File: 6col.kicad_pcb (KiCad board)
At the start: 2 copper layers, 135.3 x 94.8 mm, 48 parts, among them K1 KEYSW, K10 KEYSW, K11 KEYSW, K12 KEYSW, K13 KEYSW, K14 KEYSW, K15 KEYSW, K16 KEYSW, K17 KEYSW, K18 KEYSW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

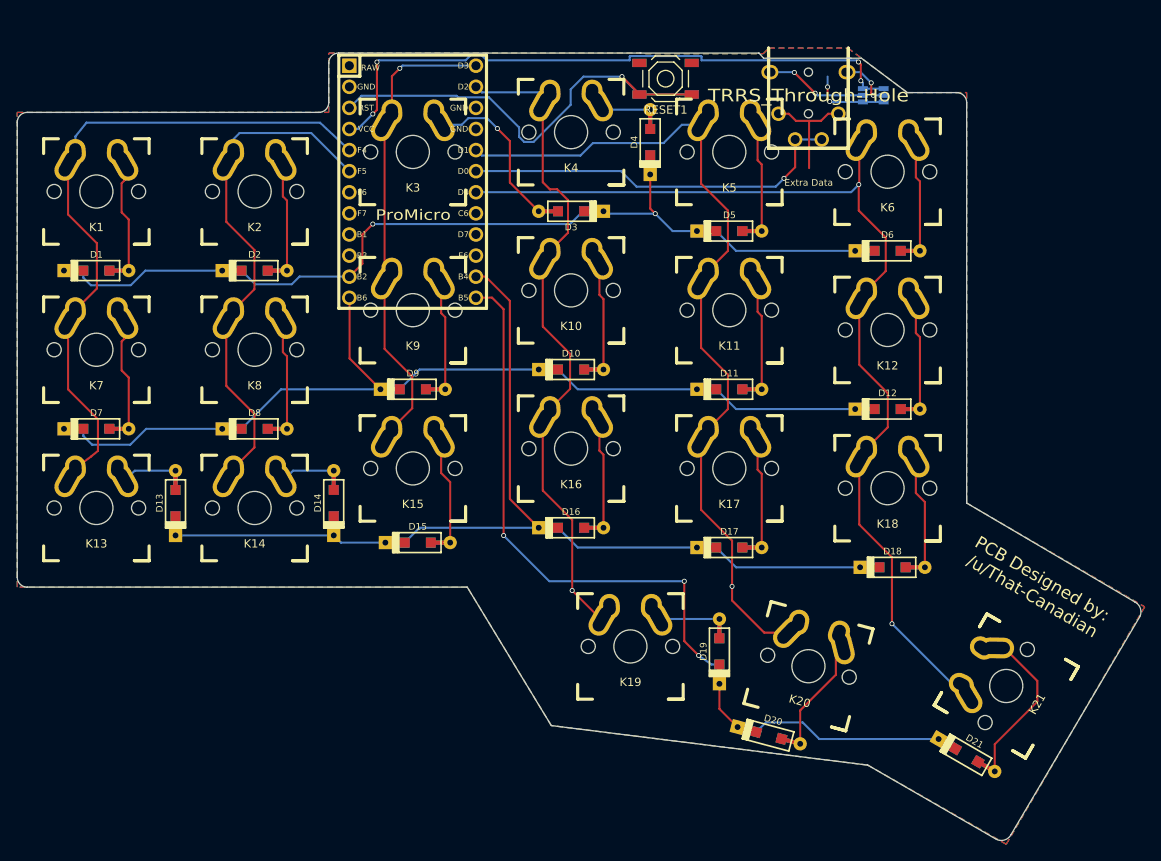
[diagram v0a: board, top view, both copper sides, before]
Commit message: WIP on Kailh sockets support
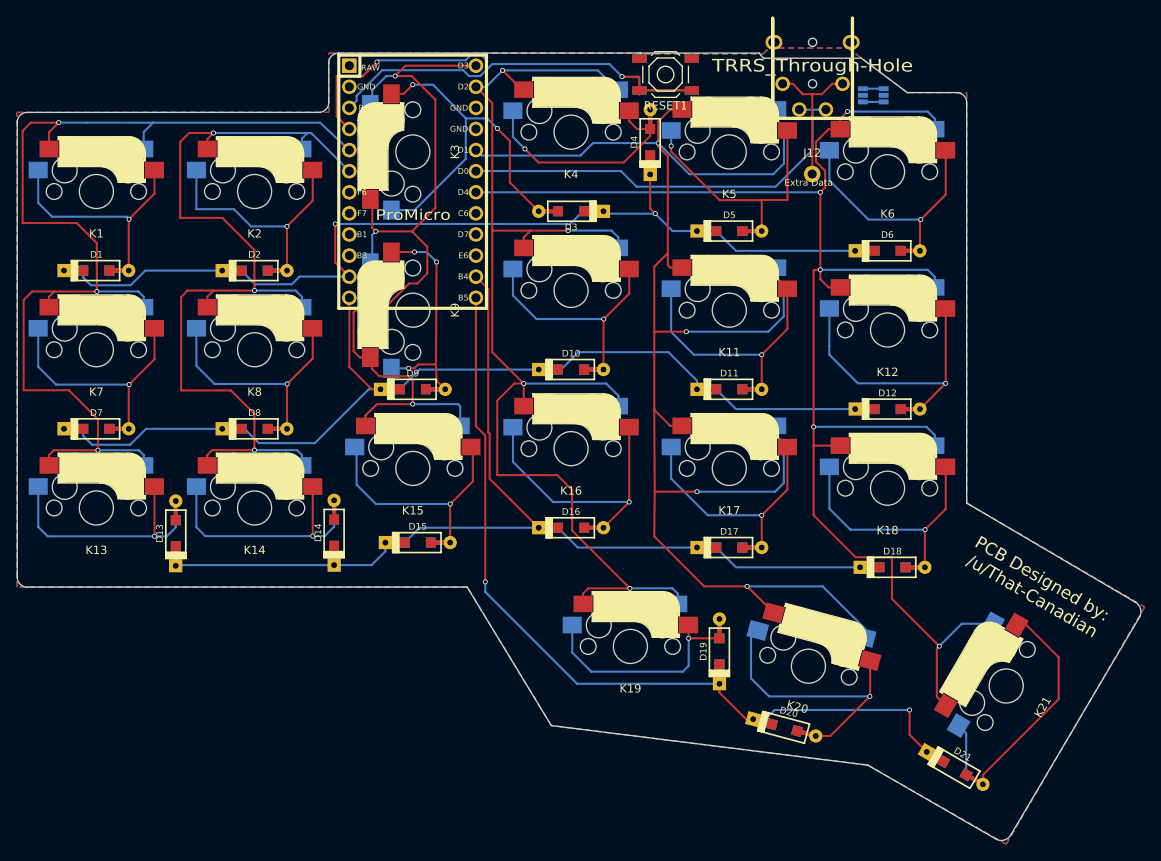
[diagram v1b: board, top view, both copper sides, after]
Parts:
- added J12: CONN_01X01_FEMALE, canadian_footprints:SolderWirePad_single_0-8mmDrill, F.Cu at (154.2, 68.9)
- K1, K10, K11, K12, K13, K14, K15, K16, K17, K18, K19, K2, K20, K3, K4, K5, K6, K7, K8, K9: value KEYSW -> KAILH_SK; footprint canadian_footprints:Mx_Alps_100-dualside -> kbd:CherryMX_Hotswap_lrn
- K21: value KEYSW -> KAILH_SK; footprint canadian_footprints:Mx_Alps_175-dualside -> kbd:CherryMX_Hotswap_lrn
- moved D13 3.65 mm to (77.5, 112.1)
- moved K22 3.63 mm to (154.2, 50.1)
- moved D14 3.57 mm to (96.6, 112.0)
- moved D21 2.11 mm to (171.3, 140.4)
- moved D20 2.10 mm to (150.8, 135.5)
- moved RESET1 0.50 mm to (136.5, 56.9) (x2)
- turned K3 to 90 degrees
- turned K9 to 90 degrees
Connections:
- K1 pad 1: /col1 -> Net-(D1-Pad2)
- K1 pad 2: Net-(D1-Pad2) -> /col1
- K10 pad 1: /col4 -> Net-(D10-Pad2)
- K10 pad 2: Net-(D10-Pad2) -> /col4
- K11 pad 1: /col5 -> Net-(D11-Pad2)
- K11 pad 2: Net-(D11-Pad2) -> /col5
- K12 pad 1: /col6 -> Net-(D12-Pad2)
- K12 pad 2: Net-(D12-Pad2) -> /col6
- K13 pad 1: /col1 -> Net-(D13-Pad2)
- K13 pad 2: Net-(D13-Pad2) -> /col1
- K14 pad 1: /col2 -> Net-(D14-Pad2)
- K14 pad 2: Net-(D14-Pad2) -> /col2
- K15 pad 1: /col3 -> Net-(D15-Pad2)
- K15 pad 2: Net-(D15-Pad2) -> /col3
- K16 pad 1: /col4 -> Net-(D16-Pad2)
- K16 pad 2: Net-(D16-Pad2) -> /col4
- K17 pad 1: /col5 -> Net-(D17-Pad2)
- K17 pad 2: Net-(D17-Pad2) -> /col5
- K18 pad 1: /col6 -> Net-(D18-Pad2)
- K18 pad 2: Net-(D18-Pad2) -> /col6
- K19 pad 1: /col4 -> Net-(D19-Pad2)
- K19 pad 2: Net-(D19-Pad2) -> /col4
- K2 pad 1: /col2 -> Net-(D2-Pad2)
- K2 pad 2: Net-(D2-Pad2) -> /col2
- K20 pad 1: /col5 -> Net-(D20-Pad2)
- K20 pad 2: Net-(D20-Pad2) -> /col5
- K21 pad 1: /col6 -> Net-(D21-Pad2)
- K21 pad 2: Net-(D21-Pad2) -> /col6
- K3 pad 1: /col3 -> Net-(D3-Pad2)
- K3 pad 2: Net-(D3-Pad2) -> /col3
- K4 pad 1: /col4 -> Net-(D4-Pad2)
- K4 pad 2: Net-(D4-Pad2) -> /col4
- K5 pad 1: /col5 -> Net-(D5-Pad2)
- K5 pad 2: Net-(D5-Pad2) -> /col5
- K6 pad 1: /col6 -> Net-(D6-Pad2)
- K6 pad 2: Net-(D6-Pad2) -> /col6
- K7 pad 1: /col1 -> Net-(D7-Pad2)
- K7 pad 2: Net-(D7-Pad2) -> /col1
- K8 pad 1: /col2 -> Net-(D8-Pad2)
- K8 pad 2: Net-(D8-Pad2) -> /col2
- K9 pad 1: /col3 -> Net-(D9-Pad2)
- K9 pad 2: Net-(D9-Pad2) -> /col3
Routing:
- net /col5: track 97.6 -> 190.5 mm, vias 1 -> 4
- net /col4: track 76.2 -> 147.8 mm, vias 1 -> 4
- net /col6: track 119.9 -> 184.8 mm, vias 2 -> 5
- net /col1: track 77.3 -> 133.1 mm, vias 0 -> 3
- net /col2: track 57.6 -> 110.9 mm, vias 0 -> 3
- net VCC: track 75.6 -> 28.9 mm, vias 4 -> 1
- net /col3: track 54.0 -> 100.1 mm, vias 1 -> 3
- net Net-(D3-Pad2): track 19.6 -> 43.4 mm, vias 1 -> 2
- net Net-(D14-Pad2): track 6.63 -> 29.2 mm, vias 0 -> 1
- net Net-(D13-Pad2): track 6.63 -> 29.1 mm, vias 0 -> 1
- net Net-(D12-Pad2): track 13.0 -> 34.4 mm, vias 0 -> 1
- net Net-(D4-Pad2): track 6.35 -> 27.5 mm, vias 0 -> 1
- net Net-(D16-Pad2): track 13.0 -> 33.6 mm, vias 0 -> 1
- net Net-(D20-Pad2): track 13.7 -> 34.1 mm, vias 0 -> 1
- net Net-(D19-Pad2): track 7.37 -> 27.2 mm, vias 0 -> 1
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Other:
- rule trace_min: 0.2 -> 0.127

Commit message: WIP on new TRRS position
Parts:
- K22: value TRRS_Through-Hole -> TRRS
- renumbered J12 to REF**
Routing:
- net VCC: track 28.9 -> 75.9 mm
- net GND: track 2.50 -> 25.5 mm, vias 0 -> 3
- net Net-(K22-Pad4): track 0.00 -> 17.5 mm, vias 0 -> 2
- net Net-(K22-Pad1): track 0.00 -> 10.2 mm
- net /col3: track 100.1 -> 97.7 mm
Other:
- board size 135.3 x 94.8 mm -> 135.3 x 97.8 mm
